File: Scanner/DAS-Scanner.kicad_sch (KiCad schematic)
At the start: 33 parts, among them J1 TETST_PORT, J2 ANT, J3 LOG_PORT, J4 PWR_PORT, P1 USB_C_Plug_USB2.0, P2 USB_C_Plug_USB2.0, SW1 SW_Push, U1 CH585M, U2 ME6210A33M3G, Y1 32.768kHz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

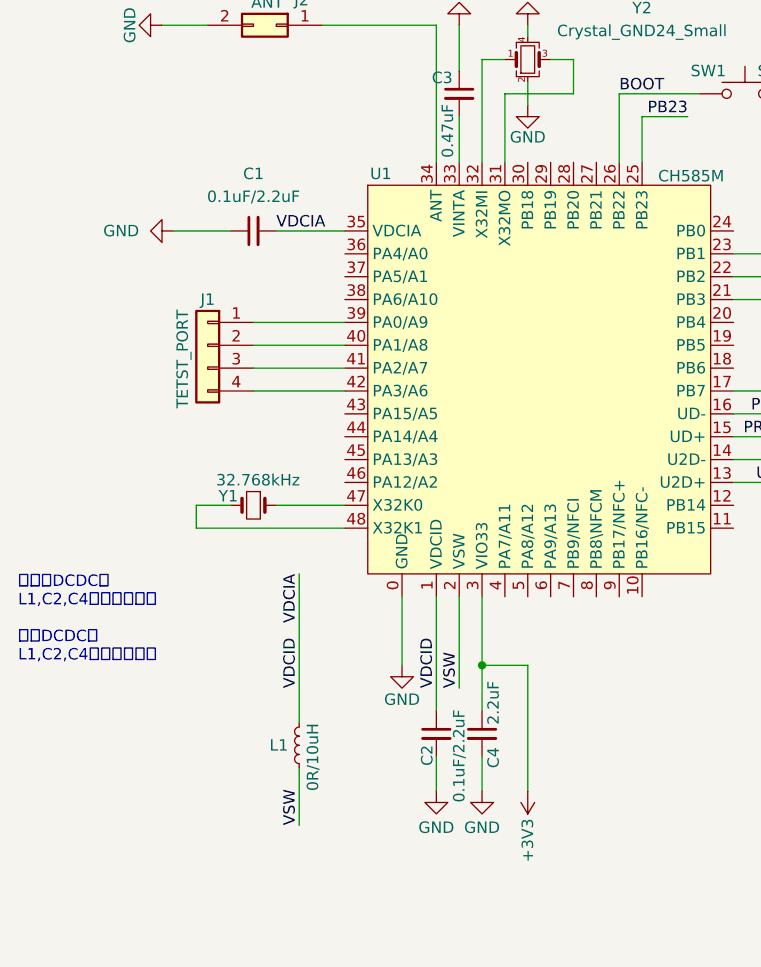
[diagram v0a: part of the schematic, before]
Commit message: fix DCDC related value desc
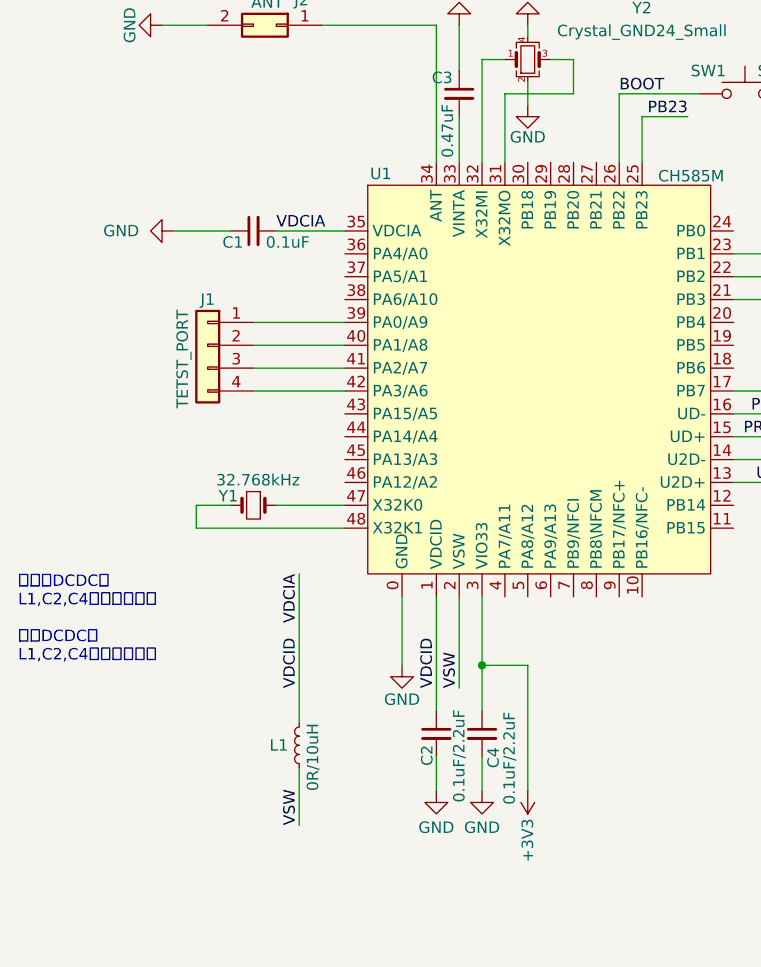
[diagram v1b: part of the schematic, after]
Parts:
- C1: value 0.1uF/2.2uF -> 0.1uF
- C4: value 2.2uF -> 0.1uF/2.2uF
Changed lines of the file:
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@@
 			)
 		)
-		(property "Value" "2.2uF"
-			(at 72.39 123.444 90)
+		(property "Value" "0.1uF/2.2uF"
+			(at 74.168 132.334 90)
 			(effects
 				(font
@@
 		(on_board yes)
 		(dnp no)
-		(fields_autoplaced yes)
 		(property "Reference" "C1"
-			(at 45.7263 62.23 90)
-			(effects
-				(font
-					(size 1.27 1.27)
-				)
-			)
-		)
-		(property "Value" "0.1uF/2.2uF"
-			(at 45.7263 64.77 90)
-			(effects
-				(font
+			(at 43.434 69.85 90)
+			(effects
+				(font
+					(size 1.27 1.27)
+				)
+			)
+		)
+		(property "Value" "0.1uF"
+			(at 49.53 69.85 90)
+			(effects
+				(font

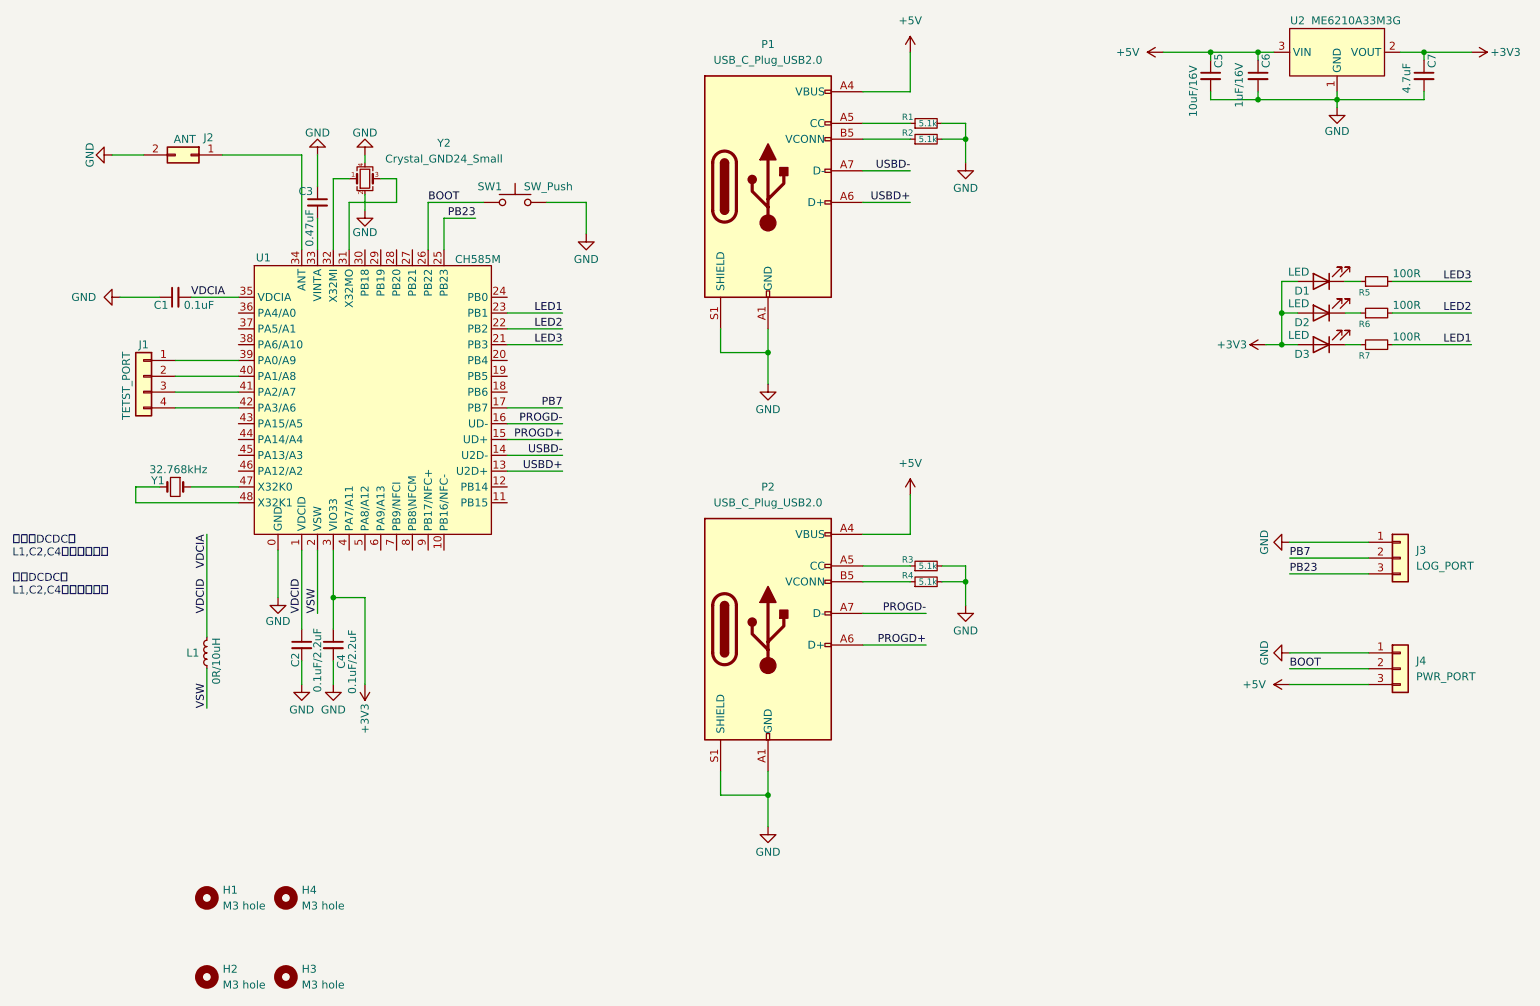
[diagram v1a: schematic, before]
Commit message: Scanner layout update
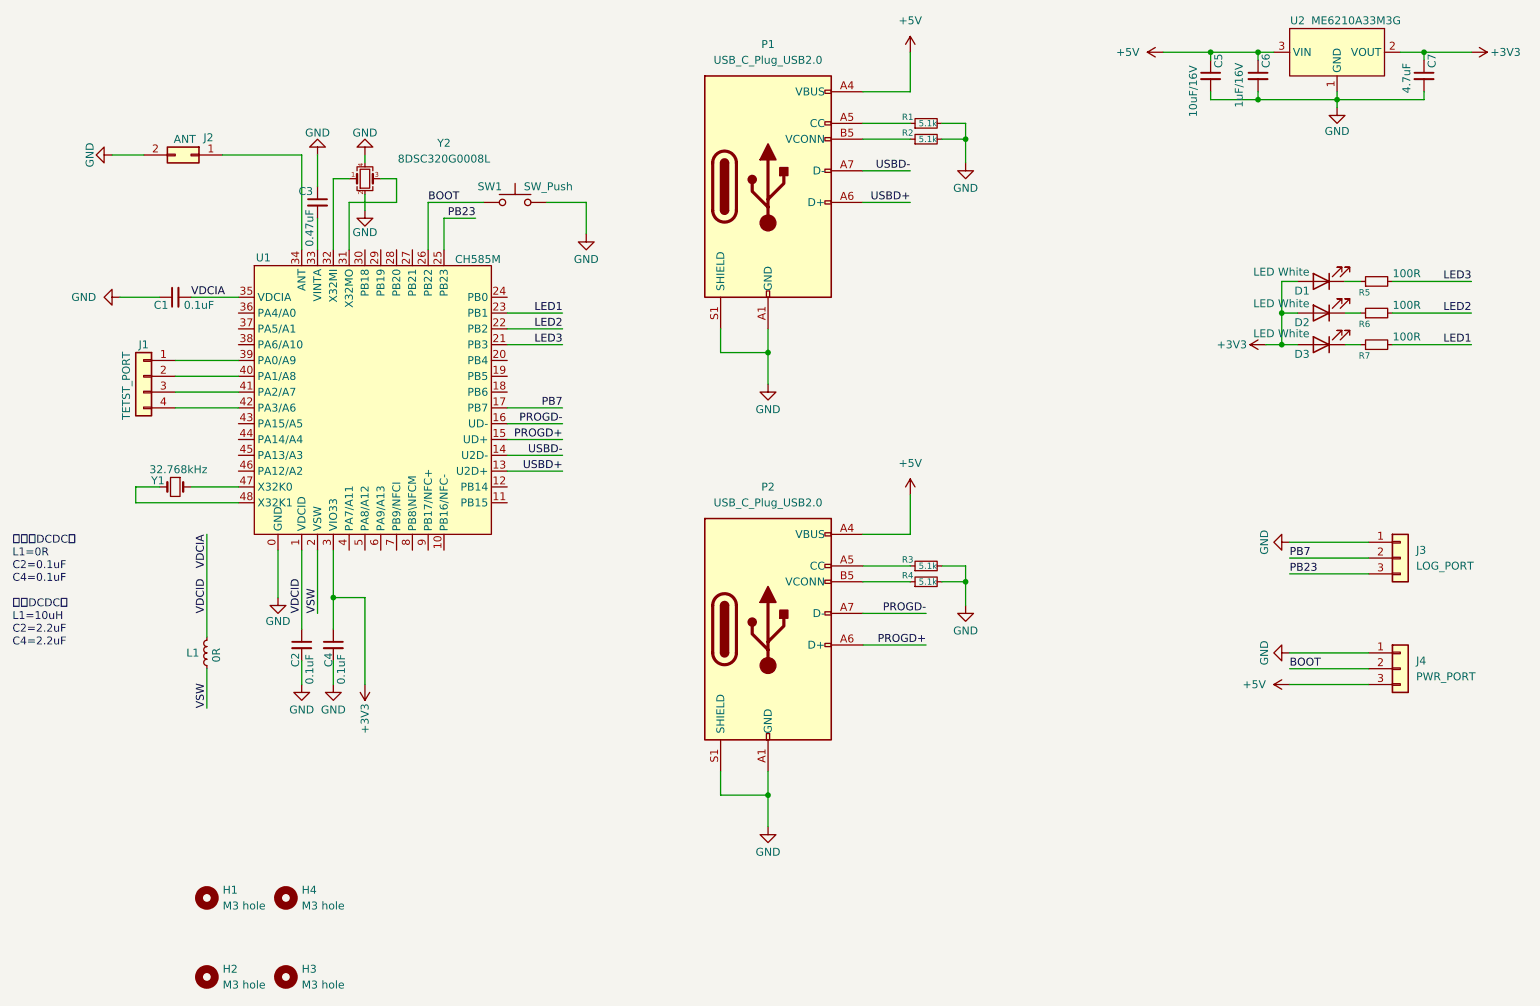
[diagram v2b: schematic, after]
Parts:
- C2, C4: value 0.1uF/2.2uF -> 0.1uF
- D1, D2, D3: value LED -> LED White
- J1, J2, J3, J4: now left out of the parts list
- L1: value 0R/10uH -> 0R
- Y2: value Crystal_GND24_Small -> 8DSC320G0008L
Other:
- note added: "不使用DCDC时 L1=0R C2=0.1uF C4=0.1uF 使用DCDC时 L1=10uH C2=2.2uF C4=2.2uF"
- note removed: "不使用DCDC时 L1,C2,C4使用第一参数 使用DCDC时 L1,C2,C4使用第二参数"
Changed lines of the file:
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@@
 	(generator_version "9.0")
 	(paper "A4")
-	(text "不使用DCDC时\nL1,C2,C4使用第一参数\n\n使用DCDC时\nL1,C2,C4使用第二参数"
+	(text "不使用DCDC时\nL1=0R\nC2=0.1uF\nC4=0.1uF\n\n使用DCDC时\nL1=10uH\nC2=2.2uF\nC4=2.2uF\n"
 		(exclude_from_sim no)
 		(at 19.558 106.934 0)
@@
 		(unit 1)
 		(exclude_from_sim no)
-		(in_bom yes)
+		(in_bom no)
 		(on_board yes)
 		(dnp no)
@@
 		(unit 1)
 		(exclude_from_sim no)
-		(in_bom yes)
+		(in_bom no)
 		(on_board yes)
 		(dnp no)
@@
 			)
 		)
-		(property "Value" "Crystal_GND24_Small"
+		(property "Value" "8DSC320G0008L"
 			(at 88.9 46.3482 0)
 			(effects
@@
 		(dnp no)
 		(property "Reference" "C4"
-			(at 72.39 128.27 90)
+			(at 70.358 128.016 90)
 			(effects
 				(font
@@
 			)
 		)
-		(property "Value" "0.1uF/2.2uF"
-			(at 74.168 132.334 90)
+		(property "Value" "0.1uF"
+			(at 72.39 130.81 90)
 			(effects
 				(font
@@
 			)
 		)
-		(property "Value" "LED"
-			(at 224.536 69.596 0)
+		(property "Value" "LED White"
+			(at 218.948 69.596 0)
 			(effects
 				(font
@@
 		(unit 1)
 		(exclude_from_sim no)
-		(in_bom yes)
+		(in_bom no)
 		(on_board yes)
 		(dnp no)
@@
 			)
 		)
-		(property "Value" "LED"
-			(at 224.536 74.676 0)
+		(property "Value" "LED White"
+			(at 218.948 74.422 0)
 			(effects
 				(font
@@
 			)
 		)
-		(property "Value" "LED"
-			(at 224.536 64.516 0)
+		(property "Value" "LED White"
+			(at 218.948 64.516 0)
 			(effects
 				(font
@@
 			)
 		)
-		(property "Value" "0R/10uH"
-			(at 52.324 130.81 90)
+		(property "Value" "0R"
+			(at 52.324 127.254 90)
 			(effects
 				(font
@@
 			)
 		)
-		(property "Value" "0.1uF/2.2uF"
-			(at 68.58 132.08 90)
+		(property "Value" "0.1uF"
+			(at 67.31 130.81 90)
 			(effects
 				(font
@@
 		(unit 1)
 		(exclude_from_sim no)
-		(in_bom yes)
+		(in_bom no)
 		(on_board yes)
 		(dnp no)
